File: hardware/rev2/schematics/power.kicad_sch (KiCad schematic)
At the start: 36 parts, among them IC1 L5970D013TR, IC2 L5970D013TR, J3 RAPC722BK

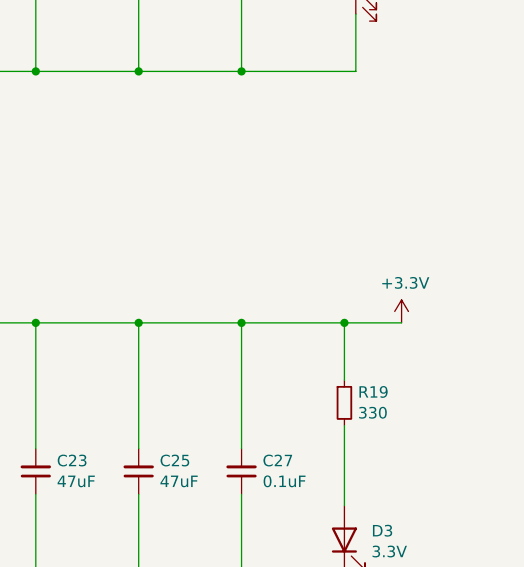
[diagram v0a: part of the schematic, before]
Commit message: ERC fixes, part 1
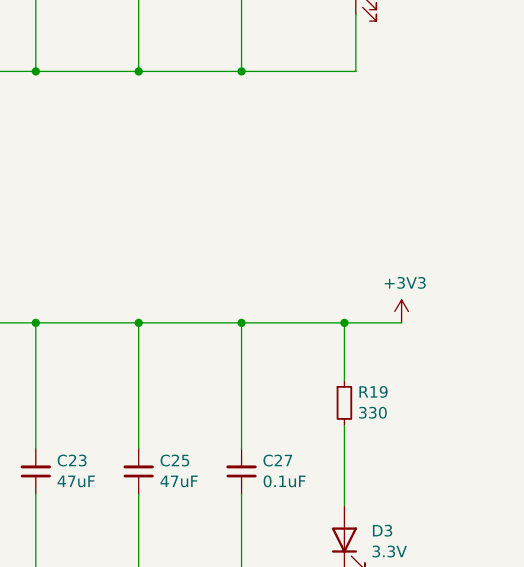
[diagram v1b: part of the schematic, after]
